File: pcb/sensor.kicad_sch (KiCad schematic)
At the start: 4 parts, among them U1 DPS368XTSA1

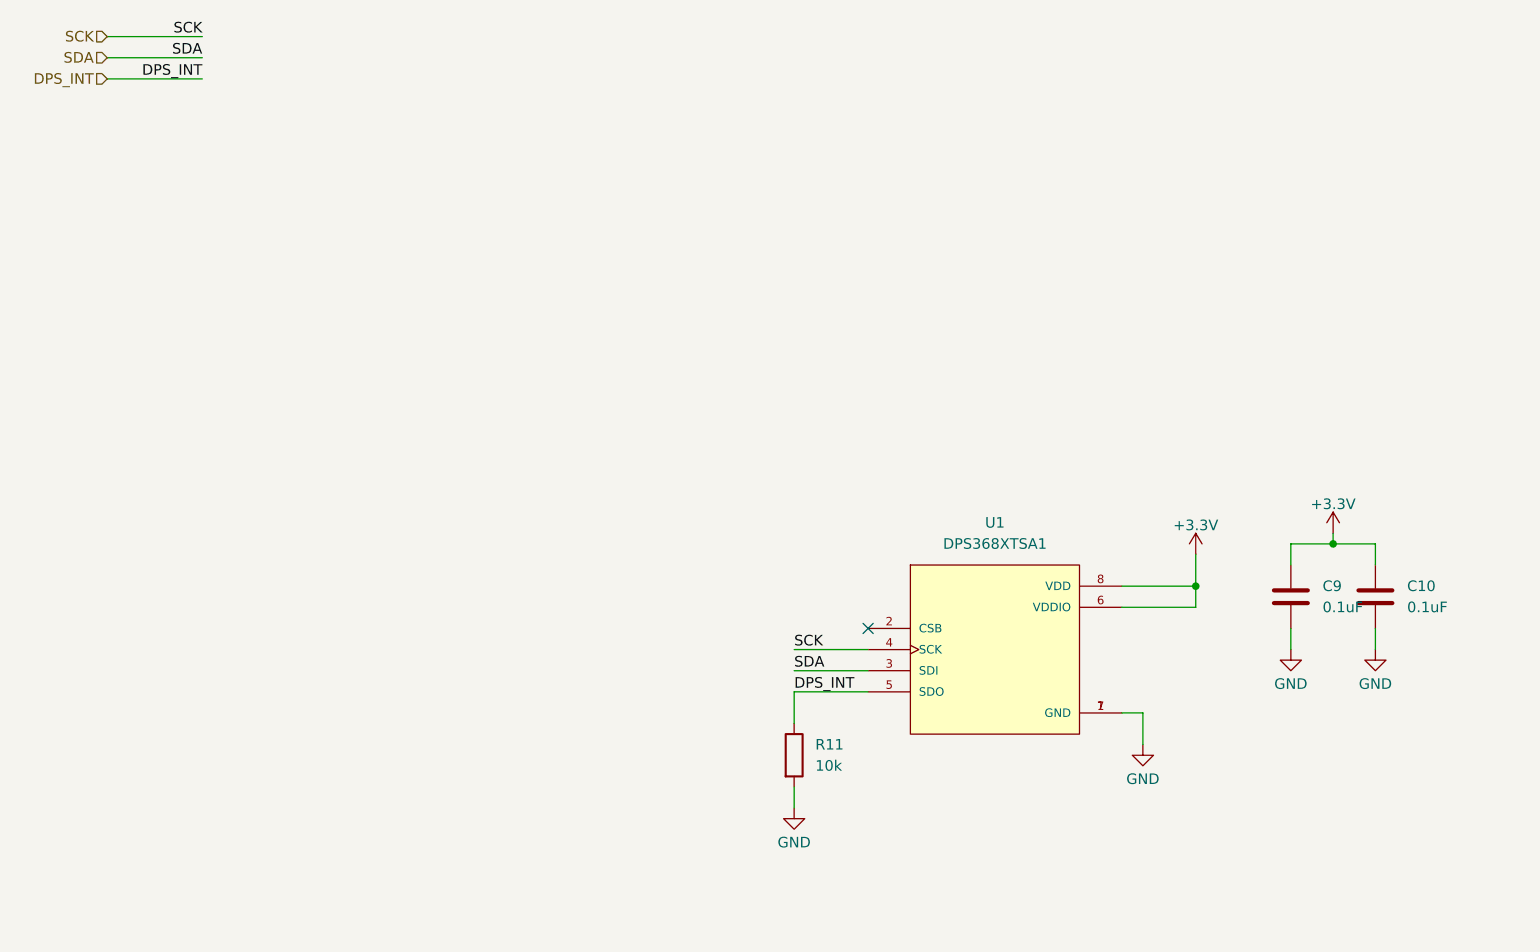
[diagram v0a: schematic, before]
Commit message: Refactored layout + silkscreen + added I2C connector
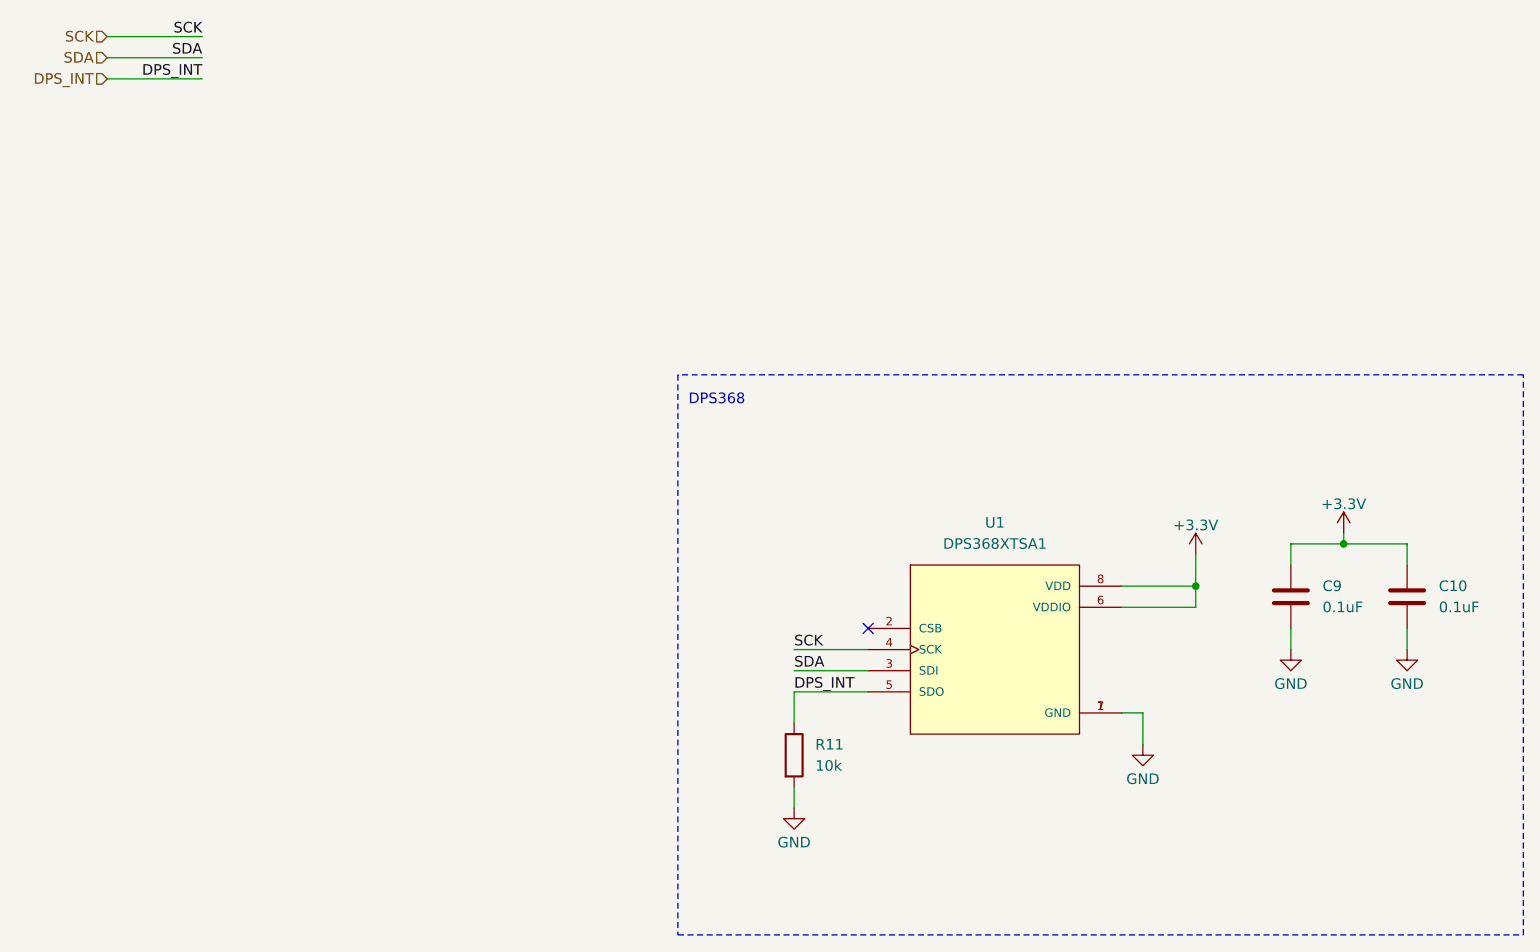
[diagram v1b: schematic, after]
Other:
- note added: "DPS368"
- moved on the sheet: C10
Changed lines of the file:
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@@
 (kicad_sch (version 20230121) (generator eeschema)
   (paper "A4")
-  (junction (at 172.72 78.74) (diameter 0) (color 0 0 0 0)
+  (junction (at 173.99 78.74) (diameter 0) (color 0 0 0 0)
   )
   (junction (at 156.21 83.82) (diameter 0) (color 0 0 0 0)
   )
   (no_connect (at 116.84 88.9))
-  (wire (pts (xy 177.8 81.28) (xy 177.8 78.74))
-    (stroke (width 0) (type default))
-  )
-  (wire (pts (xy 177.8 88.9) (xy 177.8 91.44))
-    (stroke (width 0) (type default))
-  )
-  (wire (pts (xy 167.64 78.74) (xy 172.72 78.74))
+  (wire (pts (xy 181.61 81.28) (xy 181.61 78.74))
+    (stroke (width 0) (type default))
+  )
+  (wire (pts (xy 181.61 88.9) (xy 181.61 91.44))
+    (stroke (width 0) (type default))
+  )
+  (wire (pts (xy 167.64 78.74) (xy 173.99 78.74))
     (stroke (width 0) (type default))
   )
@@
     (stroke (width 0) (type default))
   )
+  (polyline (pts (xy 195.58 125.73) (xy 195.58 58.42))
+    (stroke (width 0) (type dash))
+  )
   (wire (pts (xy 107.95 93.98) (xy 116.84 93.98))
     (stroke (width 0) (type default))
@@
     (stroke (width 0) (type default))
   )
+  (polyline (pts (xy 195.58 58.42) (xy 93.98 58.42))
+    (stroke (width 0) (type dash))
+  )
   (wire (pts (xy 107.95 96.52) (xy 116.84 96.52))
     (stroke (width 0) (type default))
@@
     (stroke (width 0) (type default))
   )
+  (wire (pts (xy 173.99 78.74) (xy 181.61 78.74))
+    (stroke (width 0) (type default))
+  )
   (wire (pts (xy 167.64 88.9) (xy 167.64 91.44))
     (stroke (width 0) (type default))
   )
-  (wire (pts (xy 172.72 78.74) (xy 172.72 77.47))
-    (stroke (width 0) (type default))
+  (wire (pts (xy 173.99 78.74) (xy 173.99 77.47))
+    (stroke (width 0) (type default))
+  )
+  (polyline (pts (xy 93.98 58.42) (xy 93.98 125.73))
+    (stroke (width 0) (type dash))
   )
   (wire (pts (xy 167.64 81.28) (xy 167.64 78.74))
     (stroke (width 0) (type default))
   )
+  (polyline (pts (xy 93.98 125.73) (xy 195.58 125.73))
+    (stroke (width 0) (type dash))
+  )
   (wire (pts (xy 107.95 91.44) (xy 116.84 91.44))
     (stroke (width 0) (type default))
@@
     (stroke (width 0) (type default))
   )
-  (wire (pts (xy 177.8 78.74) (xy 172.72 78.74))
-    (stroke (width 0) (type default))
+  (text "DPS368" (at 95.25 62.23 0)
+    (effects (font (size 1.27 1.27)) (justify left bottom))
   )
   (label "SCK" (at 36.83 17.78 180) (fields_autoplaced)
@@
     )
   )
-  (symbol (lib_id "power:GND") (at 177.8 91.44 0) (unit 1)
-    (in_bom yes) (on_board yes) (dnp no) (fields_autoplaced)
-    (property "Reference" "#PWR027" (at 177.8 97.79 0)
-      (effects (font (size 1.27 1.27)) hide)
-    )
-    (property "Value" "GND" (at 177.8 95.5755 0)
-      (effects (font (size 1.27 1.27)))
-    )
-    (property "Footprint" "" (at 177.8 91.44 0)
-      (effects (font (size 1.27 1.27)) hide)
-    )
-    (property "Datasheet" "" (at 177.8 91.44 0)
+  (symbol (lib_id "power:GND") (at 181.61 91.44 0) (unit 1)
+    (in_bom yes) (on_board yes) (dnp no) (fields_autoplaced)
+    (property "Reference" "#PWR027" (at 181.61 97.79 0)
+      (effects (font (size 1.27 1.27)) hide)
+    )
+    (property "Value" "GND" (at 181.61 95.5755 0)
+      (effects (font (size 1.27 1.27)))
+    )
+    (property "Footprint" "" (at 181.61 91.44 0)
+      (effects (font (size 1.27 1.27)) hide)
+    )
+    (property "Datasheet" "" (at 181.61 91.44 0)
       (effects (font (size 1.27 1.27)) hide)
     )
@@
     )
   )
-  (symbol (lib_id "power:+3.3V") (at 172.72 77.47 0) (unit 1)
-    (in_bom yes) (on_board yes) (dnp no) (fields_autoplaced)
-    (property "Reference" "#PWR026" (at 172.72 81.28 0)
-      (effects (font (size 1.27 1.27)) hide)
-    )
-    (property "Value" "+3.3V" (at 172.72 73.9681 0)
-      (effects (font (size 1.27 1.27)))
-    )
-    (property "Footprint" "" (at 172.72 77.47 0)
-      (effects (font (size 1.27 1.27)) hide)
-    )
-    (property "Datasheet" "" (at 172.72 77.47 0)
+  (symbol (lib_id "power:+3.3V") (at 173.99 77.47 0) (unit 1)
+    (in_bom yes) (on_board yes) (dnp no) (fields_autoplaced)
+    (property "Reference" "#PWR026" (at 173.99 81.28 0)
+      (effects (font (size 1.27 1.27)) hide)
+    )
+    (property "Value" "+3.3V" (at 173.99 73.9681 0)
+      (effects (font (size 1.27 1.27)))
+    )
+    (property "Footprint" "" (at 173.99 77.47 0)
+      (effects (font (size 1.27 1.27)) hide)
+    )
+    (property "Datasheet" "" (at 173.99 77.47 0)
       (effects (font (size 1.27 1.27)) hide)
     )
@@
     )
   )
-  (symbol (lib_id "Device:C") (at 177.8 85.09 0) (unit 1)
-    (in_bom yes) (on_board yes) (dnp no) (fields_autoplaced)
-    (property "Reference" "C10" (at 181.61 83.82 0)
-      (effects (font (size 1.27 1.27)) (justify left))
-    )
-    (property "Value" "0.1uF" (at 181.61 86.36 0)
-      (effects (font (size 1.27 1.27)) (justify left))
-    )
-    (property "Footprint" "Capacitor_SMD:C_0603_1608Metric" (at 178.7652 88.9 0)
-      (effects (font (size 1.27 1.27)) hide)
-    )
-    (property "Datasheet" "~" (at 177.8 85.09 0)
-      (effects (font (size 1.27 1.27)) hide)
-    )
+  (symbol (lib_id "Device:C") (at 181.61 85.09 0) (unit 1)
+    (in_bom yes) (on_board yes) (dnp no) (fields_autoplaced)
+    (property "Reference" "C10" (at 185.42 83.82 0)
+      (effects (font (size 1.27 1.27)) (justify left))
+    )
+    (property "Value" "0.1uF" (at 185.42 86.36 0)
+      (effects (font (size 1.27 1.27)) (justify left))
+    )
+    (property "Footprint" "Capacitor_SMD:C_0603_1608Metric" (at 182.5752 88.9 0)
+      (effects (font (size 1.27 1.27)) hide)
+    )
+    (property "Datasheet" "~" (at 181.61 85.09 0)
+      (effects (font (size 1.27 1.27)) hide)
+    )
